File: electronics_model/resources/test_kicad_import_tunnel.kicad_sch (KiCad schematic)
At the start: 3 parts

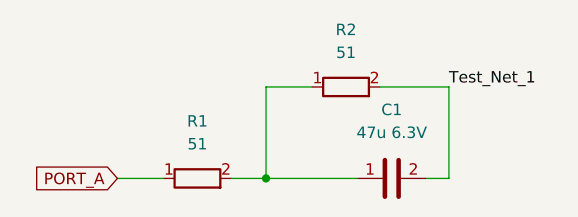
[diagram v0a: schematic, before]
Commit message: KiCad Schematic Import (#183)
Instead of importing netlists, this now directly imports schematics and
netlists from that. There are 3 methods:
- Block defined in HDL, connectivity loaded from KiCad using refdes.
- Block defined in KiCad using inline Python
- Block defined in KiCad, where the Block class defines symbol parsing
rules (eg, resistor with value "51" is parsed as a 51-ohm resistor +/- a
default tolerance of 5%)

Also adds a more general infrastructure to add KiCad value parsing rules
and symbol pin mapping rules to any block, through superclasses
KiCadInstantiableBlock (creates a Block model from a KiCad symbol) and
KiCadImportableBlock (defines symbol pinning) respectively.

Notes
- Infrastructure and unit tests only, no libraries or full examples use
this (yet).
- The netlist-from-schematic recognizes symbols, connected pins, and
labels on nets (including labels used as tunnels).
- The netlist-from-schematic isn't perfect, it doesn't detect
intersections.
- Adds parsing rules for resistors (resistance), capacitors
(capacitance, voltage), and opamps (no parameters).
- Refactors some utils in PartsTable (in electronics_abstract_parts) to
be used in the symbol parser (in the base package electronics_model)
- This replaces the kinparse (KiCad netlist parser) dependency with
sexpdata (s-expression parser). Bonus, it doesn't leave hanging open
files!
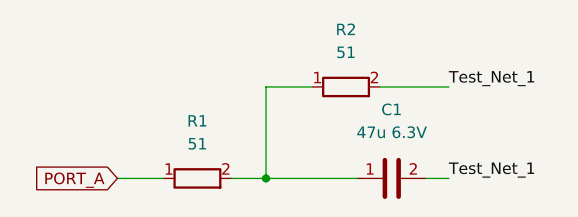
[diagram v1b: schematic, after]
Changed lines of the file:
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@@
-    (stroke (width 0) (type default) (color 0 0 0 0))
-  )
-  (wire (pts (xy 111.76 86.36) (xy 111.76 96.52))
     (stroke (width 0) (type default) (color 0 0 0 0))
   )
@@
     (stroke (width 0) (type default) (color 0 0 0 0))
   )
+  (label "Test_Net_1" (at 111.76 96.52 0)
+    (effects (font (size 1.27 1.27)) (justify left bottom))
+  )
   (label "Test_Net_1" (at 111.76 86.36 0)

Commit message: Refactor examples / libraries to use import KiCad schematics (#184)
Refactors a lot of analog blocks (most opamp topologies, analog
switches) to be KiCad importable blocks (by defining a symbol pin
mapping) and/or KiCad imported schematics. Adds custom symbols for many
of these parts, some KiCad's base symbol library for the most part lacks
abstract / generic and high-level parts.

Netlists of example designs should not have changed.

KiCad import behavior change:
- global labels must connect to either a node or external block port and
are not treated as link names
- net labels are used as link names and must not collide with any
existing object member
- add unit tests for the above
- schematic now works on a fixed grid so points can be rounded to the
nearest point that lines up - it turns out points on schematic files can
be off by like 0.05 or something which broke the previous netlister
- support power nets (eg, GND, Vcc symbols)
- power nets and all labels are treated as connected in the schematic
importer (instead of punted up to the block to be handled as connected
in separate connect statements)
- support inline modified symbols (lib_name vs lib_id)
- support symbol mirror, fix rotation calculation (and unit test all of
this)
- import blocks in schematic in xy order (or optionally file order -
this isn't used)
- add a `file_path` utility function to KiCadSchematicBlock which
returns a relative path from the calling file
- moves some tests (mainly rotation, mirror, symbol connectivity) to be
schematic parser tests only, because it's a bit extra (and probably
doesn't tell us much more) to go all the way to Block proto

Infrastructural changes:
- refactors some existing symbol mappings to use pin names instead of
numbers
- refactors some existing symbol mappings to use Mapping return type
which is type covariant
- for connection type errors (link inference errors), prints the names
of the ports involved
- some better error 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
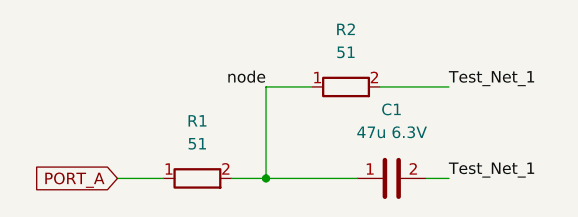
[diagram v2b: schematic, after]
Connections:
- net node: now reaches C1.1, R1.2, R2.1
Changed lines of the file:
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@@
     (stroke (width 0) (type default) (color 0 0 0 0))
+  )
+  (label "node" (at 91.44 86.36 180)
+    (effects (font (size 1.27 1.27)) (justify right bottom))
   )
   (label "Test_Net_1" (at 111.76 96.52 0)
@@
       (effects (font (size 1.27 1.27)) (justify right) hide)
     )
-  )
-  (symbol (lib_name "R_1") (lib_id "Device:R") (at 100.33 86.36 90) (unit 1)
-    (in_bom yes) (on_board yes) (fields_autoplaced)
-    (property "Reference" "R2" (id 0) (at 100.33 80.01 90))
-    (property "Value" "51" (id 1) (at 100.33 82.55 90))
-    (property "Footprint" "" (id 2) (at 100.33 88.138 90)
-      (effects (font (size 1.27 1.27)) hide)
-    )
-    (property "Datasheet" "~" (id 3) (at 100.33 86.36 0)
-      (effects (font (size 1.27 1.27)) hide)
-    )
-    (pin "1")
-    (pin "2")
   )
   (symbol (lib_id "Device:R") (at 83.82 96.52 90) (unit 1)
@@
     (pin "2")
   )
+  (symbol (lib_id "Device:R") (at 100.33 86.36 90) (unit 1)
+    (in_bom yes) (on_board yes) (fields_autoplaced)
+    (property "Reference" "R2" (id 0) (at 100.33 80.01 90))
+    (property "Value" "51" (id 1) (at 100.33 82.55 90))
+    (property "Footprint" "" (id 2) (at 100.33 88.138 90)
+      (effects (font (size 1.27 1.27)) hide)
+    )
+    (property "Datasheet" "~" (id 3) (at 100.33 86.36 0)
+      (effects (font (size 1.27 1.27)) hide)
+    )
+    (pin "1")
+    (pin "2")
+  )
   (sheet_instances
     (path "/" (page "1"))
@@
       (reference "R1") (unit 1) (value "51") (footprint "")
     )
-    (path "/053518b3-994e-4e57-8f86-80f07be5a072"
+    (path "/fe14220d-de68-4888-8844-281c4c9176a2"
       (reference "R2") (unit 1) (value "51") (footprint "")
     )

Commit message: unify naming
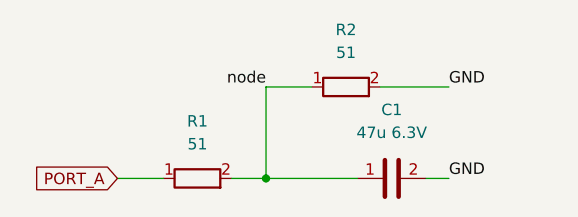
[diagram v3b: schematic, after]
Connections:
- net Test_Net_1 renamed GND
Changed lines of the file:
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@@
     (effects (font (size 1.27 1.27)) (justify right bottom))
   )
-  (label "Test_Net_1" (at 111.76 96.52 0)
+  (label "GND" (at 111.76 96.52 0)
     (effects (font (size 1.27 1.27)) (justify left bottom))
   )
-  (label "Test_Net_1" (at 111.76 86.36 0)
+  (label "GND" (at 111.76 86.36 0)
     (effects (font (size 1.27 1.27)) (justify left bottom))
   )
